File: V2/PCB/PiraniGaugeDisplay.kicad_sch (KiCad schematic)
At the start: 75 parts, among them J101 AuxIN, J102 Conn_02x03_Odd_Even, J103 RJ45, U101 AMS1117-3.3, U102 SN75176AD, U103 LM2596S-5, U104 ESP32-S3-WROOM-1(N16R2), U105 SW-SMD_L6.1-W3.5-LS8.0, U106 SW-SMD_L6.1-W3.5-LS8.0

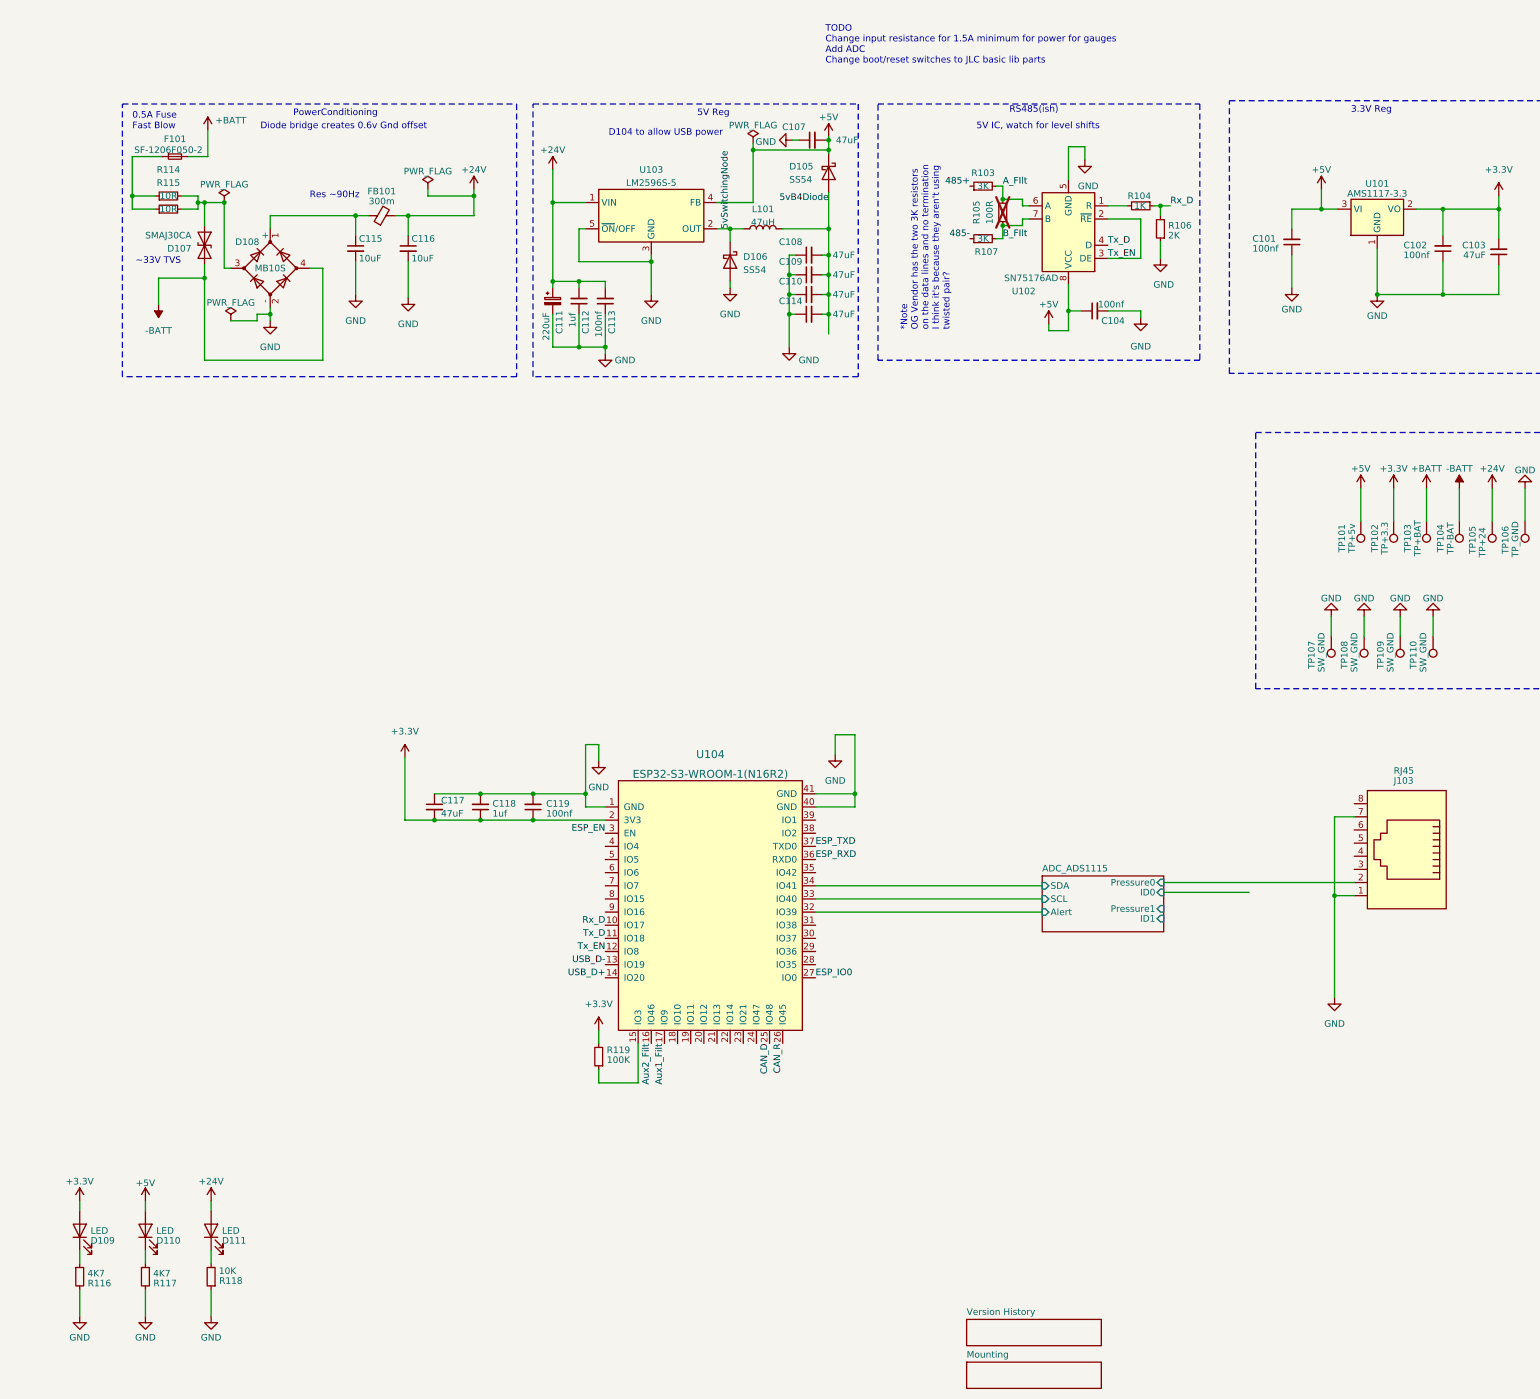
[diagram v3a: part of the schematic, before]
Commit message: added double plug
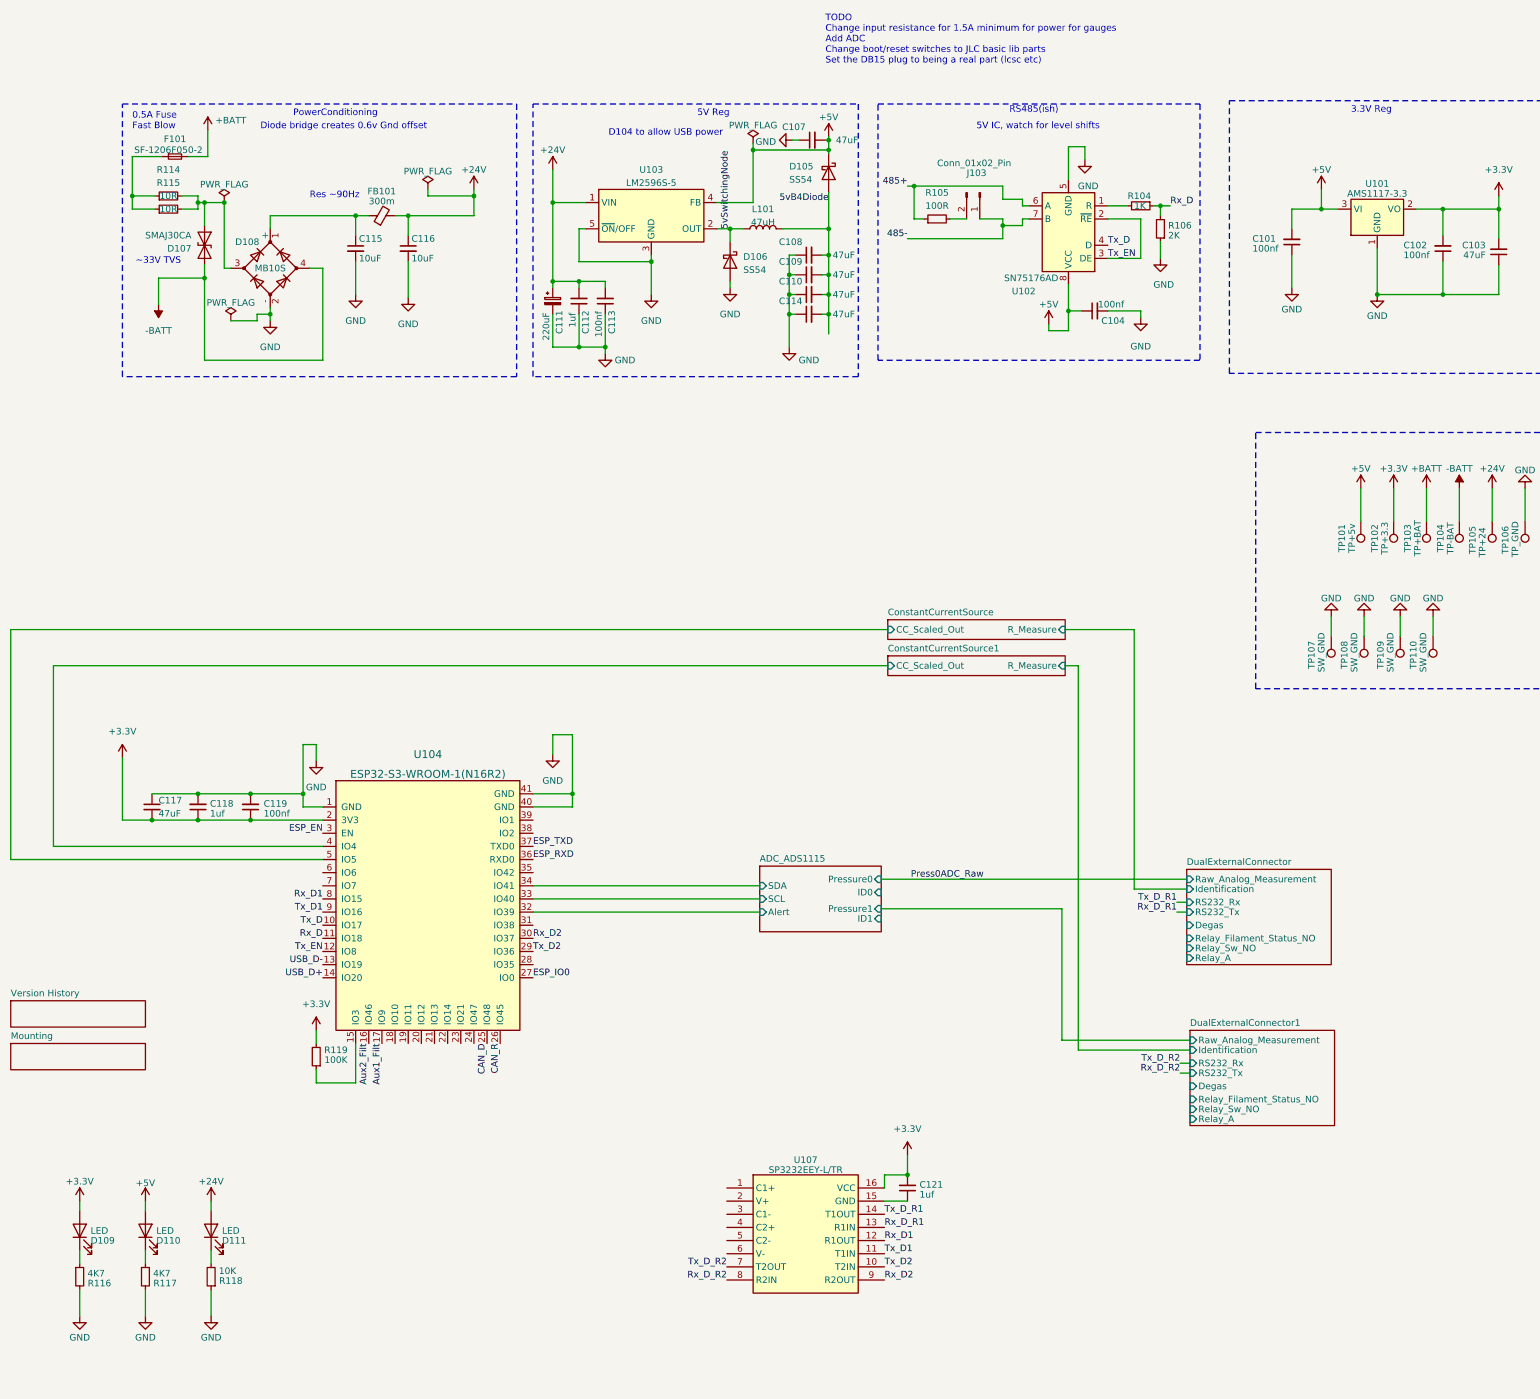
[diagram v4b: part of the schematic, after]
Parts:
- removed J103: RJ45, SamacSys_Parts:55551621, symbol PGD-Library:RJ45
- removed R103, R107: 3K, Resistor_SMD:R_0805_2012Metric, symbol PGD-Library:R_Small
- added C121: 1uf, Capacitor_SMD:C_0805_2012Metric, symbol PGD-Library:C_Small
- added J103: Conn_01x02_Pin, symbol Connector:Conn_01x02_Pin
- added U107: SP3232EEY-L/TR, easyeda2kicad2:TSSOP-16_L5.0-W4.4-P0.65-LS6.4-BL, symbol easyeda2kicad2:SP3232EEY-L_TR
- R105: now fitted
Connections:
- net +3.3V: now also C121.2, U107.16 (VCC)
- net 485+: now also R105.1, U102.6 (A)
- net 485-: now also U102.7 (B), J103.1 (Pin_1)
- net Rx_D: now also U104.11 (IO18); no longer U104.10 (IO17)
- net Tx_D: now also U104.10 (IO17); no longer U104.11 (IO18)
- net Tx_D2: now reaches U104.29 (IO36)
- net Tx_D2: now also U107.10 (T2IN)
- net Rx_D2: now reaches U104.30 (IO37)
- net Rx_D2: now also U107.9 (R2OUT)
- net ConstantCurrentSource1/CC_Scaled_Out: now reaches U104.4 (IO4)
- net ConstantCurrentSource/CC_Scaled_Out: now reaches U104.5 (IO5)
- net Rx_D1: now reaches U104.8 (IO15)
- net Rx_D1: now also U107.12 (R1OUT)
- net Tx_D1: now reaches U104.9 (IO16)
- net Tx_D1: now also U107.11 (T1IN)
- net A_FIlt: no longer names the net of R105.2
- net A_FIlt: now also J103.2 (Pin_2); no longer U102.6 (A)
- removed net B_FIlt: R105.1, U102.7 (B)
- new net: C121.1, U107.15 (GND)
- new net Rx_D_R1: U107.13 (R1IN)
- new net Rx_D_R2: U107.8 (R2IN)
- new net Tx_D_R1: U107.14 (T1OUT)
- new net Tx_D_R2: U107.7 (T2OUT)
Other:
- added sheet ConstantCurrentSource (CCS.kicad_sch)
- added sheet ConstantCurrentSource1 (CCS.kicad_sch)
- added sheet DualExternalConnector (DualExternalConnector.kicad_sch)
- added sheet DualExternalConnector1 (DualExternalConnector.kicad_sch)
- note added: "TODO Change input resistance for 1.5A minimum for power for gauges Add ADC Change boot/reset switches to JLC basic lib parts Set the DB15 plug to being a real part (lcsc etc)"
- note removed: "*Note OG Vendor has the two 3K resistors on the data lines and no termination I think it's because they aren't using twisted pair?"
- note removed: "TODO Change input resistance for 1.5A minimum for power for gauges Add ADC Change boot/reset switches to JLC basic lib parts"
- moved on the sheet: C117, C118, C119, R119, U104

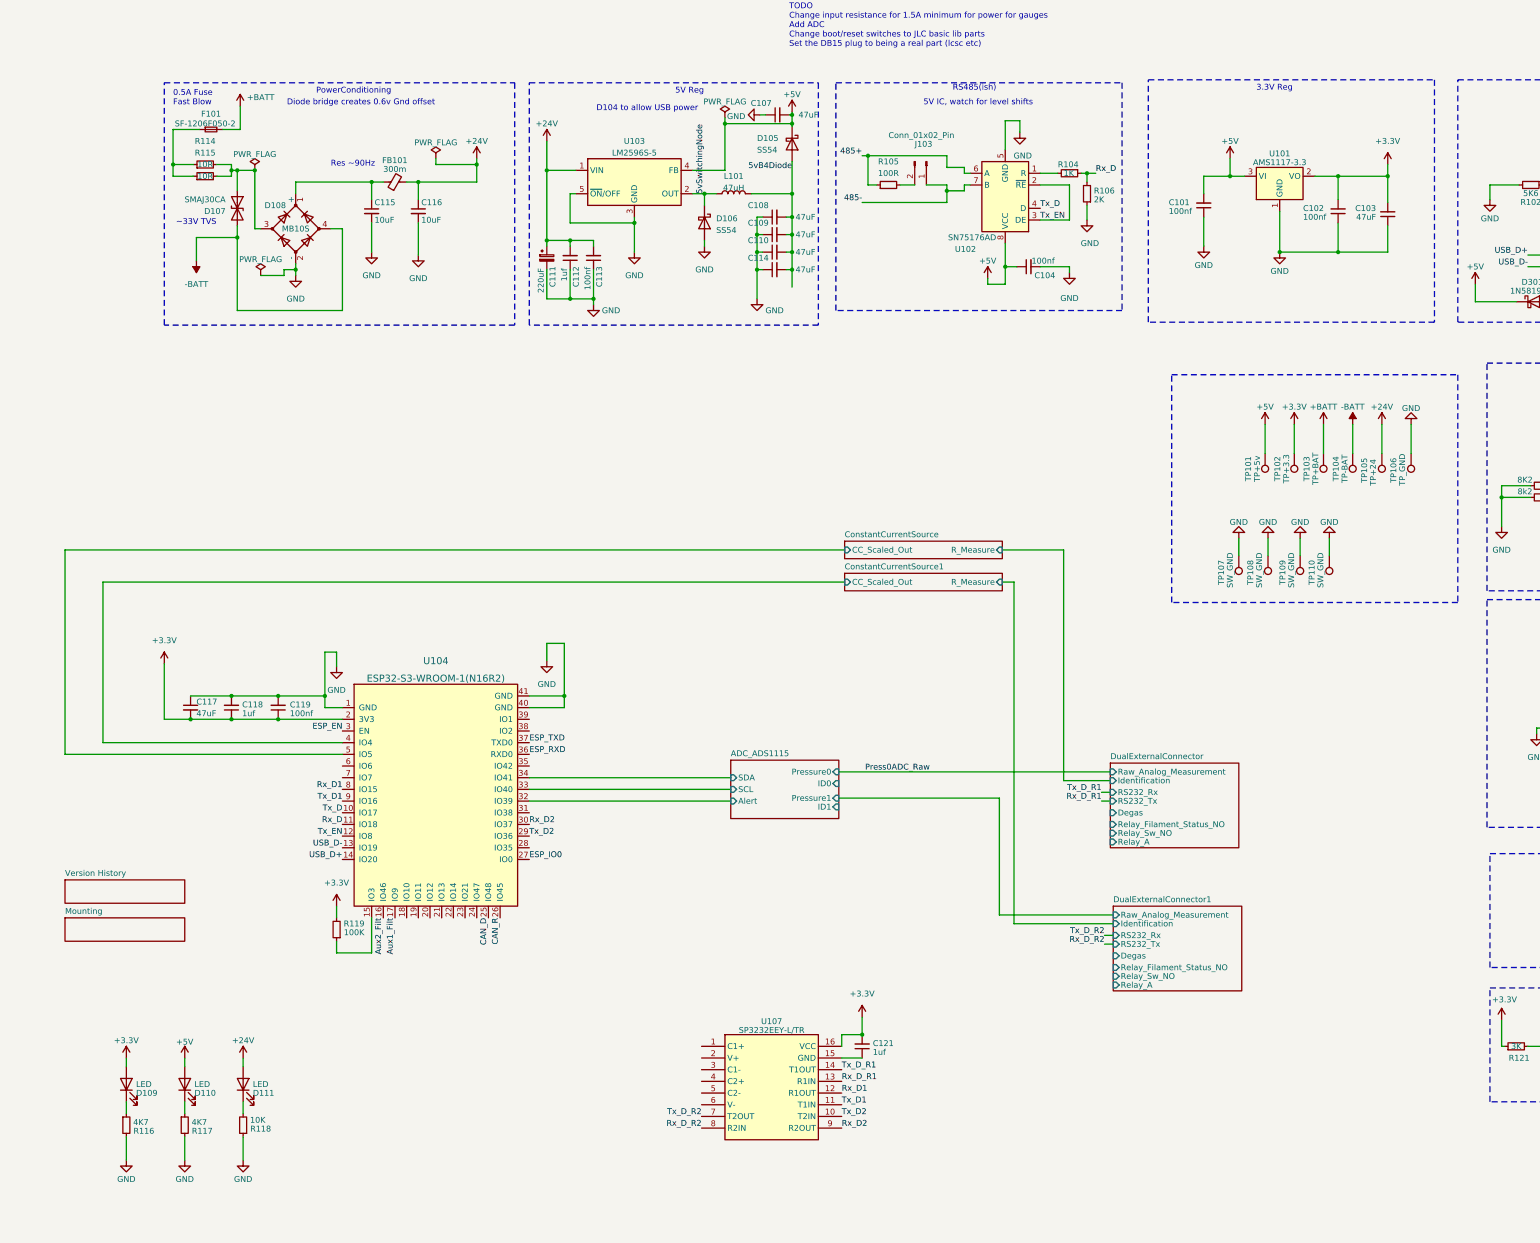
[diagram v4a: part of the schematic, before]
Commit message: added thermocouple
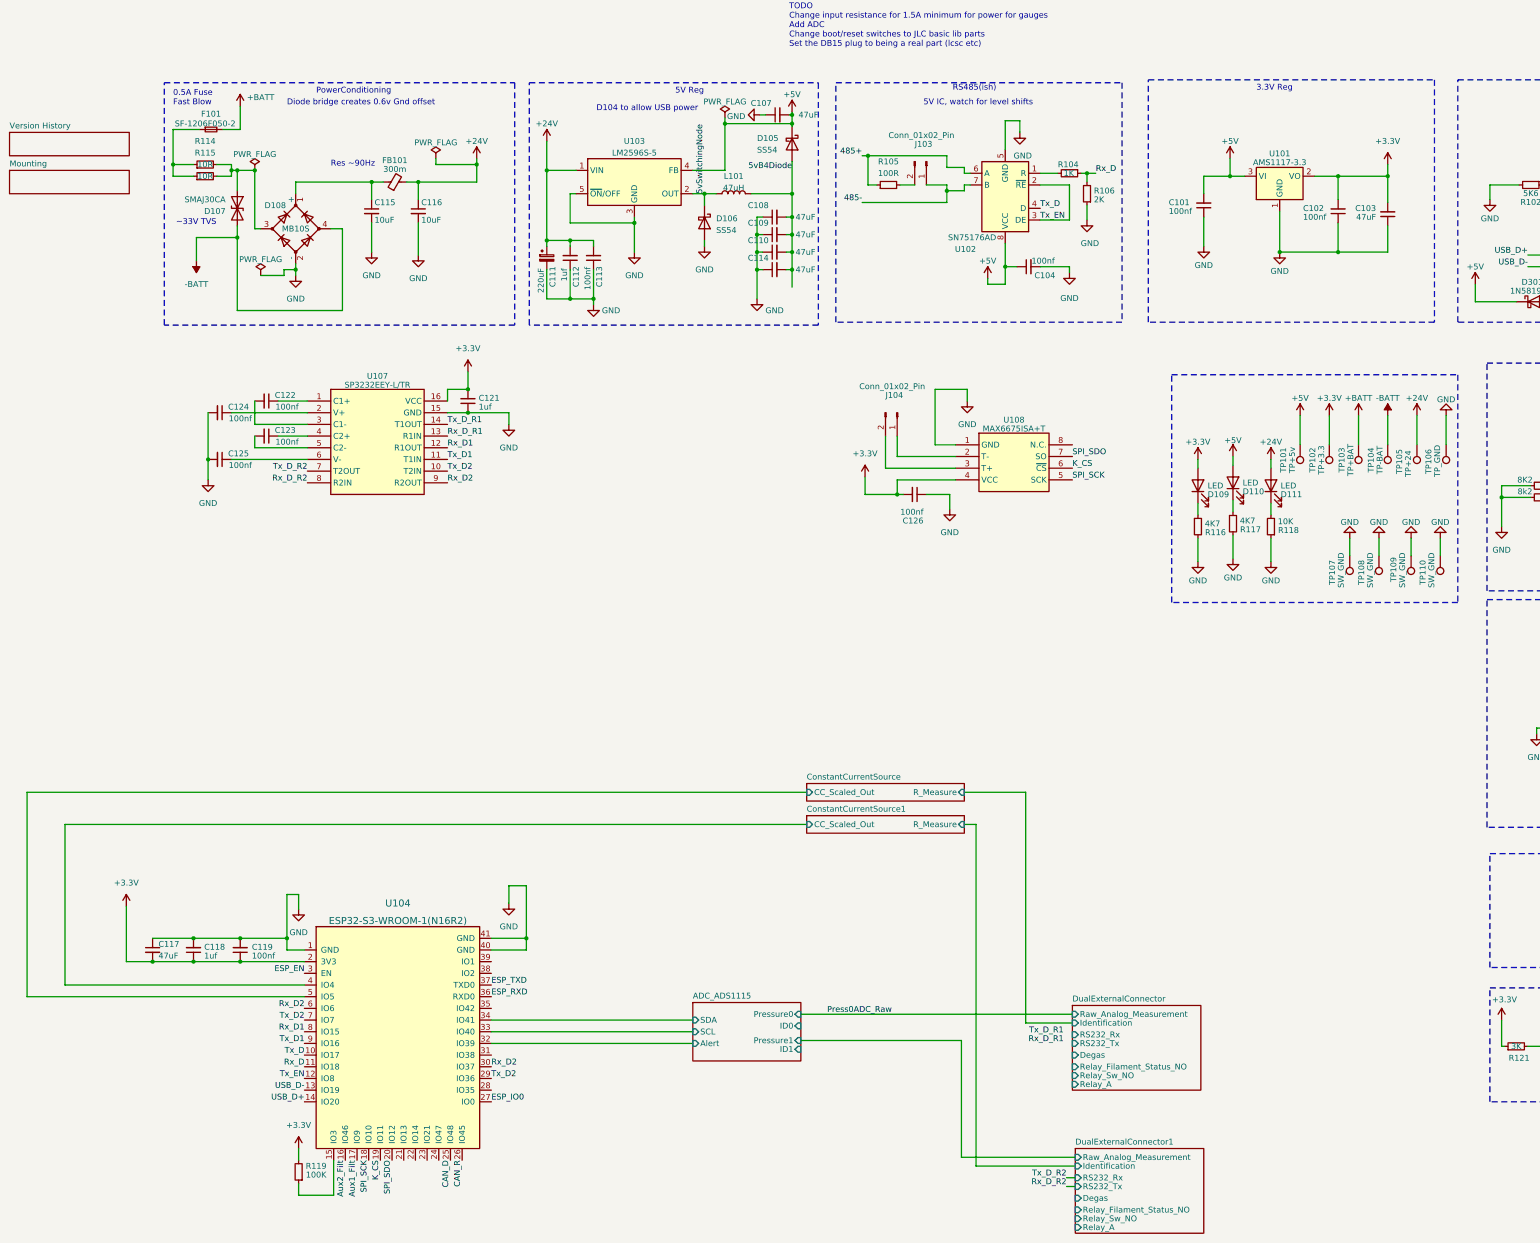
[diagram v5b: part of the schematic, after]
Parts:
- added C122, C123, C124, C125, C126: 100nf, Capacitor_SMD:C_0805_2012Metric, symbol PGD-Library:C_Small
- added J104: Conn_01x02_Pin, symbol Connector:Conn_01x02_Pin
- added U108: MAX6675ISA+T, easyeda2kicad2:SOIC-8_L5.0-W4.0-P1.27-LS6.0-BL, symbol easyeda2kicad2:MAX6675ISA+T
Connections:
- net +3.3V: now also C126.2, U108.4 (VCC)
- net GND: now also C121.1, U107.15 (GND), C124.2, C125.2, C126.1, U108.1 (GND)
- net Rx_D2: now also U104.6 (IO6)
- net Tx_D2: now also U104.7 (IO7)
- net SPI_SCK: now reaches U104.18 (IO10)
- net SPI_SCK: now also U108.5 (SCK)
- net K_CS: now reaches U104.19 (IO11)
- net K_CS: now also U108.6 (~{CS})
- net SPI_SDO: now reaches U104.20 (IO12)
- net SPI_SDO: now also U108.7 (SO)
- net at U107.1 (C1+): now also C122.1
- net at U107.2 (V+): now also C124.1
- net at U107.3 (C1-): now also C122.2
- net at U107.4 (C2+): now also C123.1
- net at U107.5 (C2-): now also C123.2
- net at U107.6 (V-): now also C125.1
- new net: J104.1 (Pin_1), U108.2 (T-)
- new net: J104.2 (Pin_2), U108.3 (T+)
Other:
- moved on the sheet: C117, C118, C119, C121, D109, D110, D111, R116, R117, R118, R119, TP101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
